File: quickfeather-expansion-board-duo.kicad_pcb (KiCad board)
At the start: 2 copper layers, 5 parts, among them J1 QuickFeather, J2 1x4_Conn, J3 1x4_Conn, J4 QuickFeather, J5 UDA1334

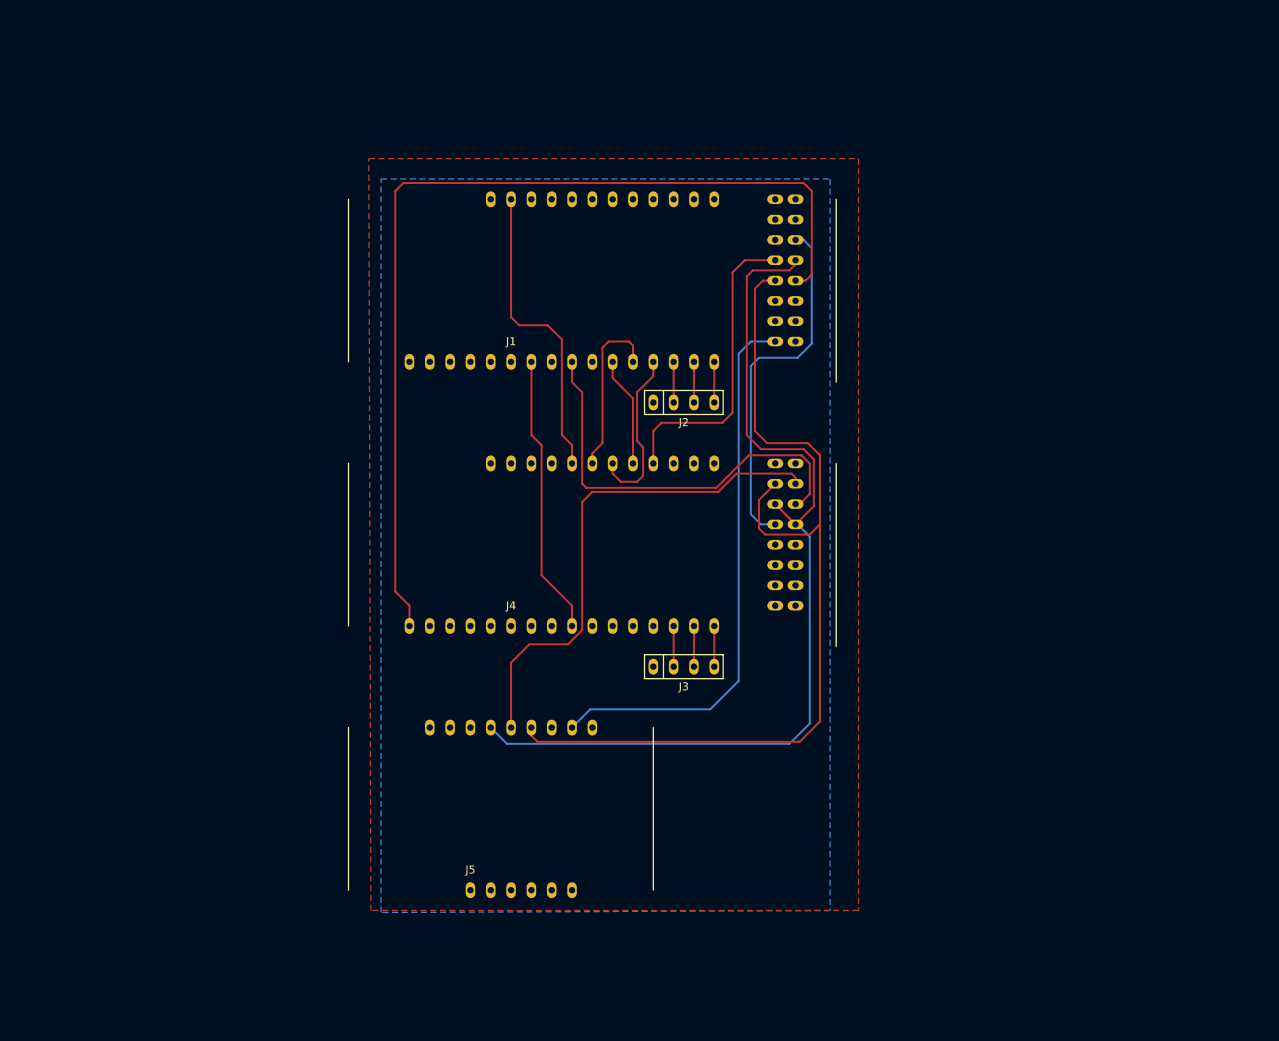
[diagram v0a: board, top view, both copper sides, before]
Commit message: 1st Rev of schematic Part Placement - partial
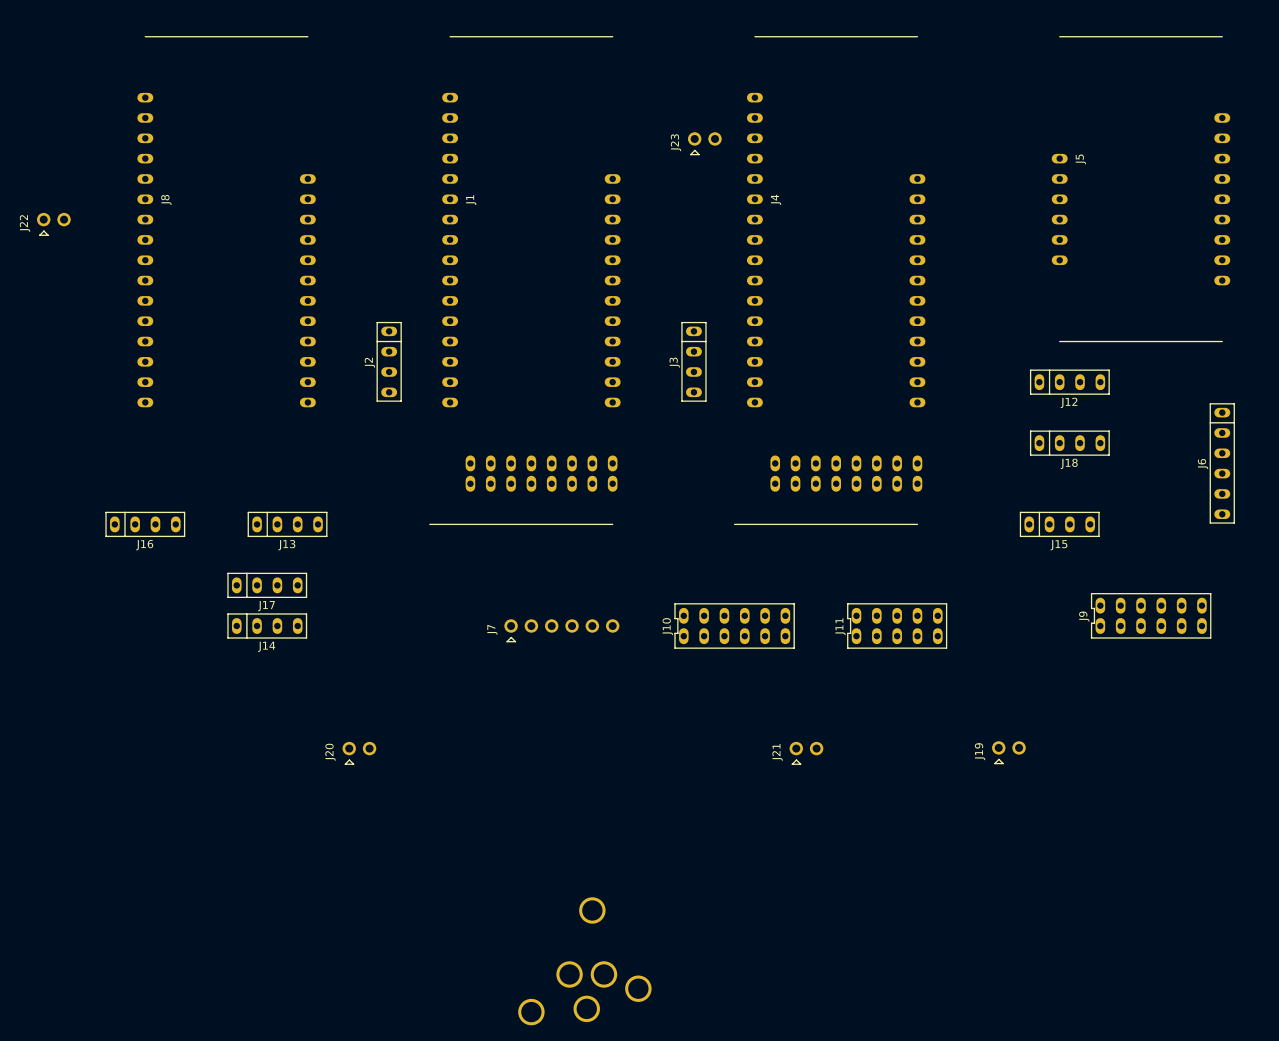
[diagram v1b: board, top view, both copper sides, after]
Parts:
- added H1: MountingHole, MPAD, F.Cu at (106.7, 147.3)
- added H2: MountingHole, MPAD, F.Cu at (99.0, 160.0)
- added H3: MountingHole, MPAD, F.Cu at (106.0, 159.6)
- added H4: MountingHole, MPAD, F.Cu at (112.4, 157.1)
- added H5: MountingHole, MPAD, F.Cu at (108.1, 155.3)
- added H6: MountingHole, MPAD, F.Cu at (103.8, 155.3)
- added J10: PMOD, quicklogicBoards-footprints:2x6_Conn, F.Cu at (124.5, 111.8)
- added J11: VM3011, quicklogicBoards-footprints:2x5_Conn, F.Cu at (144.8, 111.8)
- added J12: SCL_PU, quicklogicBoards-footprints:1x4_Conn, F.Cu at (166.4, 81.3)
- added J13: SDA_PU, quicklogicBoards-footprints:1x4_Conn, F.Cu at (68.6, 99.1)
- added J14: SCL1, quicklogicBoards-footprints:1x4_Conn, F.Cu at (66.0, 111.8)
- added J15: SCL_PU, quicklogicBoards-footprints:1x4_Conn, F.Cu at (165.1, 99.1)
- added J16: GND, quicklogicBoards-footprints:1x4_Conn, F.Cu at (50.8, 99.1)
- added J17: SDA1, quicklogicBoards-footprints:1x4_Conn, F.Cu at (66.0, 106.7)
- added J18: SDA_PU, quicklogicBoards-footprints:1x4_Conn, F.Cu at (166.4, 88.9)
- added J19: D3P3V, quicklogicBoards-footprints:1x2_Conn, F.Cu at (157.4, 124.4)
- added J20: H3P3V, quicklogicBoards-footprints:1x2_Conn, F.Cu at (76.2, 124.5)
- added J21: EXT, quicklogicBoards-footprints:1x2_Conn, F.Cu at (132.1, 124.5)
- added J22: H3V, quicklogicBoards-footprints:1x2_Conn, F.Cu at (38.0, 58.3)
- added J23: DEMO, quicklogicBoards-footprints:1x2_Conn, F.Cu at (119.4, 48.3)
- added J6: LIS2DH12, quicklogicBoards-footprints:1x6_Conn, F.Cu at (185.4, 91.4)
- added J7: eSPI_Sensor, quicklogicBoards-footprints:1x6_pinhead, F.Cu at (96.4, 109.1)
- added J8: huzzah32, quicklogicBoards-footprints:huzzah32, F.Cu at (45.7, 63.5)
- added J9: Calaveras, quicklogicBoards-footprints:2x6_Conn, F.Cu at (176.5, 110.5)
- J2: value 1x4_Conn -> H_UART
- J3: value 1x4_Conn -> D_UART
- moved J5 110.7 mm to (162.6, 58.4), turned to 270 degrees
- moved J4 57.1 mm to (121.9, 63.5), turned to 270 degrees
- moved J3 38.1 mm to (119.4, 78.7), turned to 270 degrees
- moved J2 37.2 mm to (81.3, 78.7), turned to 270 degrees
- moved J1 27.0 mm to (83.8, 63.5), turned to 270 degrees
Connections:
- J1 pad 25: Net-(J1-Pad25) -> /H_SDA
- J1 pad 26: Net-(J1-Pad26) -> /H_SCL
- J4 pad 10: Net-(J4-Pad10) -> /RC_DEMO
- J4 pad 17: Net-(J4-Pad17) -> /PDM_DATA
- J4 pad 21: Net-(J4-Pad21) -> /eSPI_MISO
- J4 pad 22: Net-(J4-Pad22) -> /eSPI_CLK
- J4 pad 23: Net-(J4-Pad23) -> /eSPI_MOSI
- J4 pad 24: Net-(J4-Pad24) -> /D3P3V
- J4 pad 25: Net-(J4-Pad25) -> /D_SDA0
- J4 pad 26: Net-(J4-Pad26) -> /D_SCL0
- J4 pad 33: Net-(J4-Pad33) -> /D_SCL1
- J4 pad 34: Net-(J4-Pad34) -> /D_SDA1
- J4 pad 35: Net-(J4-Pad35) -> /SPIm_CS2n
- J4 pad 37: Net-(J4-Pad37) -> /PDM_CLK
- J4 pad 4: Net-(J4-Pad4) -> /SPIm_MISO
- J4 pad 42: Net-(J4-Pad42) -> /eSPI_CSn
- J4 pad 5: Net-(J4-Pad5) -> /SPIm_MOSI
- J4 pad 6: Net-(J4-Pad6) -> /SPIm_CLK
- J4 pad 7: Net-(J4-Pad7) -> /INT1
- J4 pad 9: Net-(J4-Pad9) -> /WOS
- J5 pad 8: /H3P3V -> /3P3V
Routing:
- net /RESETn: track 120.8 -> 0.00 mm
- net /I2S_CLK: track 117.6 -> 0.00 mm
- net /I2S_WCLK: track 116.7 -> 0.00 mm
- net /H3P3V: track 69.3 -> 0.00 mm
- net /I2S_DOUT: track 63.8 -> 0.00 mm
- net /D2H_ACK: track 52.9 -> 0.00 mm
- net /H2D_INT: track 46.0 -> 0.00 mm
- net /D2H_INT: track 38.4 -> 0.00 mm
- net /SPI_CSn: track 38.3 -> 0.00 mm
- net /H2D_ACK: track 35.1 -> 0.00 mm
- net /SPI_MOSI: track 21.4 -> 0.00 mm
- net /SPI_MISO: track 21.2 -> 0.00 mm
- net /SPI_CLK: track 13.8 -> 0.00 mm
- net GND: track 10.2 -> 0.00 mm
- net /H_TX: track 5.08 -> 0.00 mm
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- removed copper zone on B.Cu, net GND
- removed copper zone on F.Cu, net GND

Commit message: Submit: 1. Latest layout 2. generated schematic 3. Gerber files 4. Updated layout library
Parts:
- removed H5, H6: MountingHole, MPAD
- added N1: ql_logo, quicklogicBoards-footprints:Ql_logo, F.Cu at (113.0, 100.3)
- J1: value QuickFeather -> QF HOST
- J12: value SCL_PU -> SCL1_PU
- J13: value SDA_PU -> SDA1_PU
- J15: value SCL_PU -> SCL0_PU
- J18: value SDA_PU -> SDA0_PU
- J19: value D3P3V -> H3P3V
- J20: value H3P3V -> D3P3V
- J4: value QuickFeather -> QF DEVICE
- J8: value huzzah32 -> HUZZAH32-QWIIC
- moved H3 143.1 mm to (185.4, 40.7)
- moved H4 134.2 mm to (45.7, 40.7)
- moved J19 107.7 mm to (81.4, 48.2), turned to 270 degrees
- moved H2 102.9 mm to (185.4, 104.2)
- moved J12 99.7 mm to (67.3, 92.7)
- moved J20 86.4 mm to (116.8, 48.2), turned to 270 degrees
- moved J21 86.1 mm to (50.7, 96.4)
- moved H1 74.7 mm to (45.7, 104.2)
- moved J10 43.5 mm to (81.3, 106.7)
- moved J7 23.0 mm to (119.4, 110.5), turned to 180 degrees
- moved J14 22.9 mm to (67.3, 88.9), turned to 180 degrees
- moved J17 21.1 mm to (54.6, 88.9), turned to 180 degrees
- moved J15 19.4 mm to (161.3, 80.0), turned to 180 degrees
- moved J13 15.3 mm to (54.6, 92.7)
- moved J22 14.4 mm to (48.3, 48.2), turned to 270 degrees
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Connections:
- J1 pad 15: Net-(J1-Pad15) -> /H3P3V
- J1 pad 24: /H3P3V -> Net-(J1-Pad24)
- J4 pad 15: Net-(J4-Pad15) -> /D3P3V
- J4 pad 24: /D3P3V -> Net-(J4-Pad24)
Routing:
- net /RESETn: track 0.00 -> 175.3 mm
- net /H2D_INT: track 0.00 -> 149.7 mm
- net /D2H_INT: track 0.00 -> 144.4 mm
- net /D_SDA1: track 0.00 -> 132.6 mm
- net /D_SCL0: track 0.00 -> 129.4 mm
- net /I2S_WCLK: track 0.00 -> 128.6 mm, vias 0 -> 2
- net /I2S_CLK: track 0.00 -> 121.7 mm, vias 0 -> 2
- net /SPIm_CS2n: track 0.00 -> 120.8 mm
- net /D_SDA0: track 0.00 -> 118.9 mm
- net GND: track 0.00 -> 116.2 mm
- net /SPI_CLK: track 0.00 -> 114.6 mm
- net /D_SCL1: track 0.00 -> 113.7 mm
- net /D2H_ACK: track 0.00 -> 110.6 mm
- net /SPI_CSn: track 0.00 -> 95.3 mm
- net /SPI_MOSI: track 0.00 -> 94.6 mm
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- added copper zone on B.Cu, net /3P3V
- added copper zone on F.Cu, net GND
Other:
- board outline added: 149.9 x 77.5 mm
- board text added: "QuickLogic Expansion Board Duo Rev: 1.0"
